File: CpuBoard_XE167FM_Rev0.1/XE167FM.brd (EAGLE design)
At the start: 68.3 x 50.8 mm, 40 parts, among them IC1 XE167FM, Y1 8Mhz

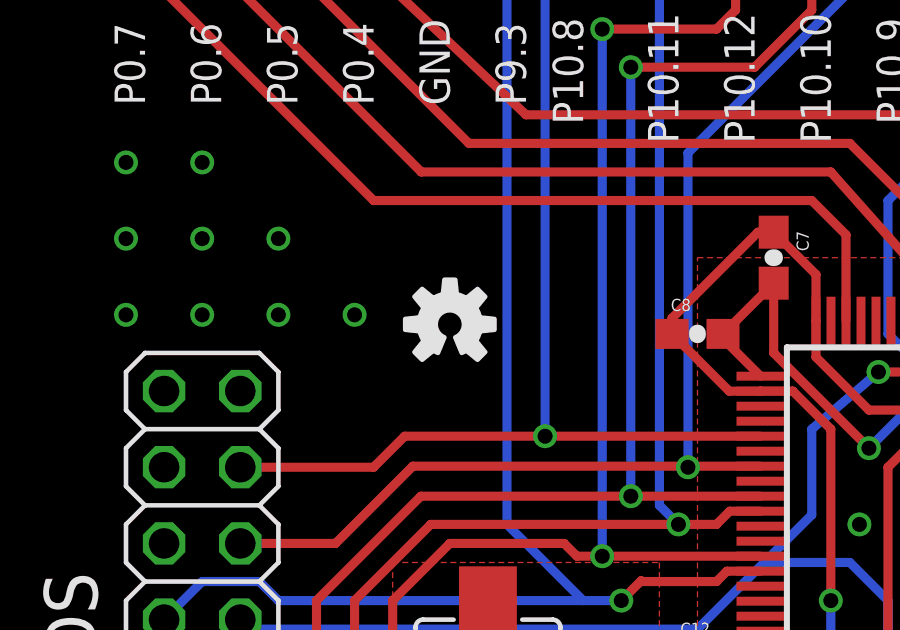
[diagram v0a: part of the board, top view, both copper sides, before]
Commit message: OSHW logo rotated
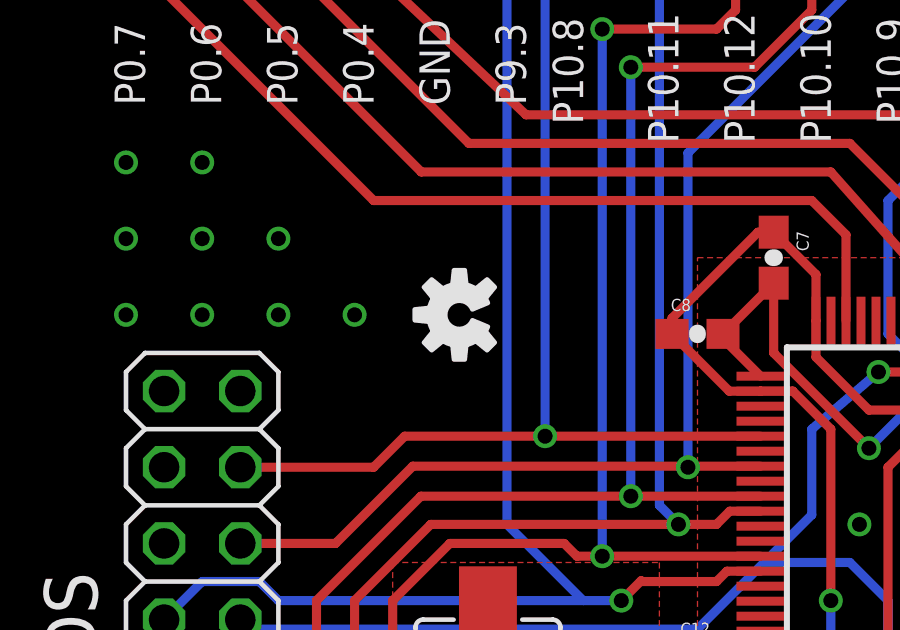
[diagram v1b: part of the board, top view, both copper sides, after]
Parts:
- moved LOGO1 0.45 mm to (13.7, 36.2), turned to 90 degrees
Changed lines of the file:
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@@
 <attribute name="NAME" x="40.7035" y="10.6045" size="0.4064" layer="25" font="vector"/>
 </element>
-<element name="LOGO1" library="SparkFun-Aesthetics" package="OSHW-LOGO-S" value="OSHW-LOGOS" x="13.335" y="35.8775"/>
+<element name="LOGO1" library="SparkFun-Aesthetics" package="OSHW-LOGO-S" value="OSHW-LOGOS" x="13.6525" y="36.195" rot="R90"/>
 </elements>
 <signals>
